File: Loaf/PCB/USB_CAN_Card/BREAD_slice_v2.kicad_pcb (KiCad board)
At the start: 2 copper layers, 100 x 70.6 mm, 8 parts, among them J1 10018783-10200TLF, U2 MCP3208

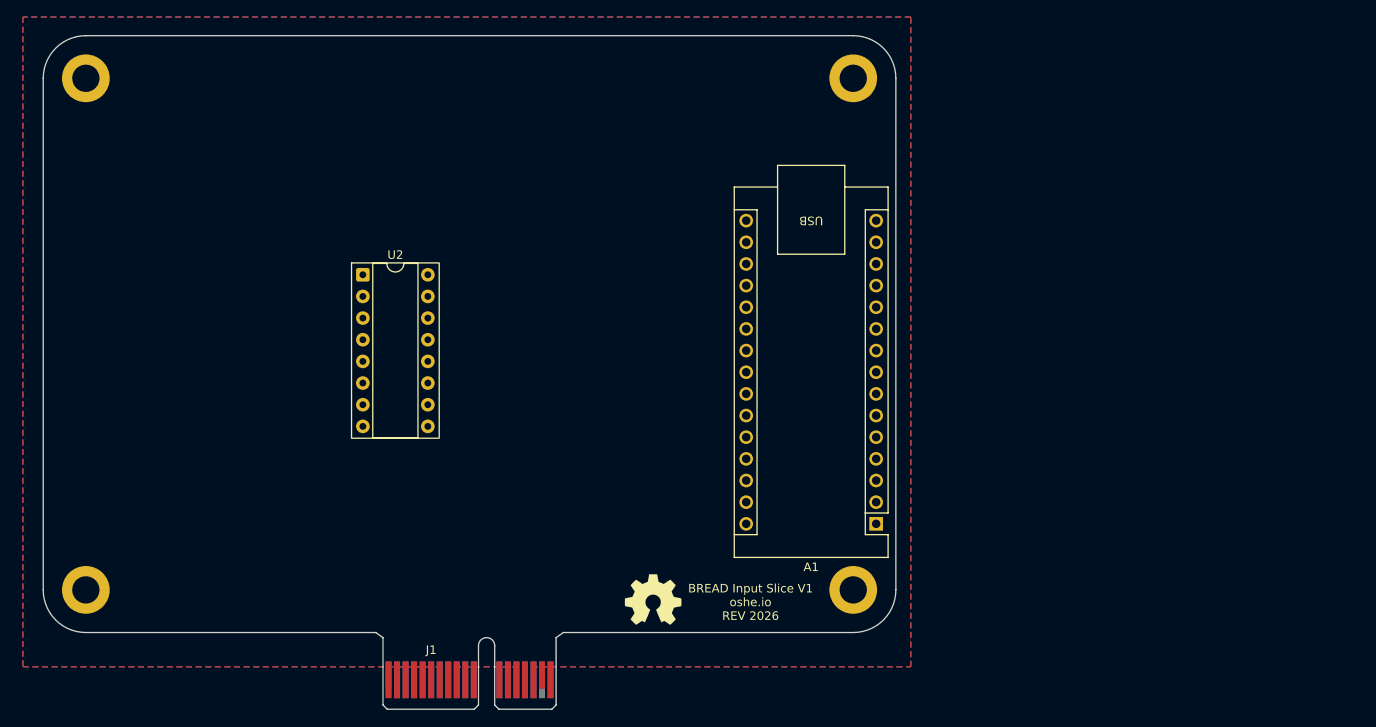
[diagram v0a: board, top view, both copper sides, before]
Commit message: Added parts to USB-CAN Card
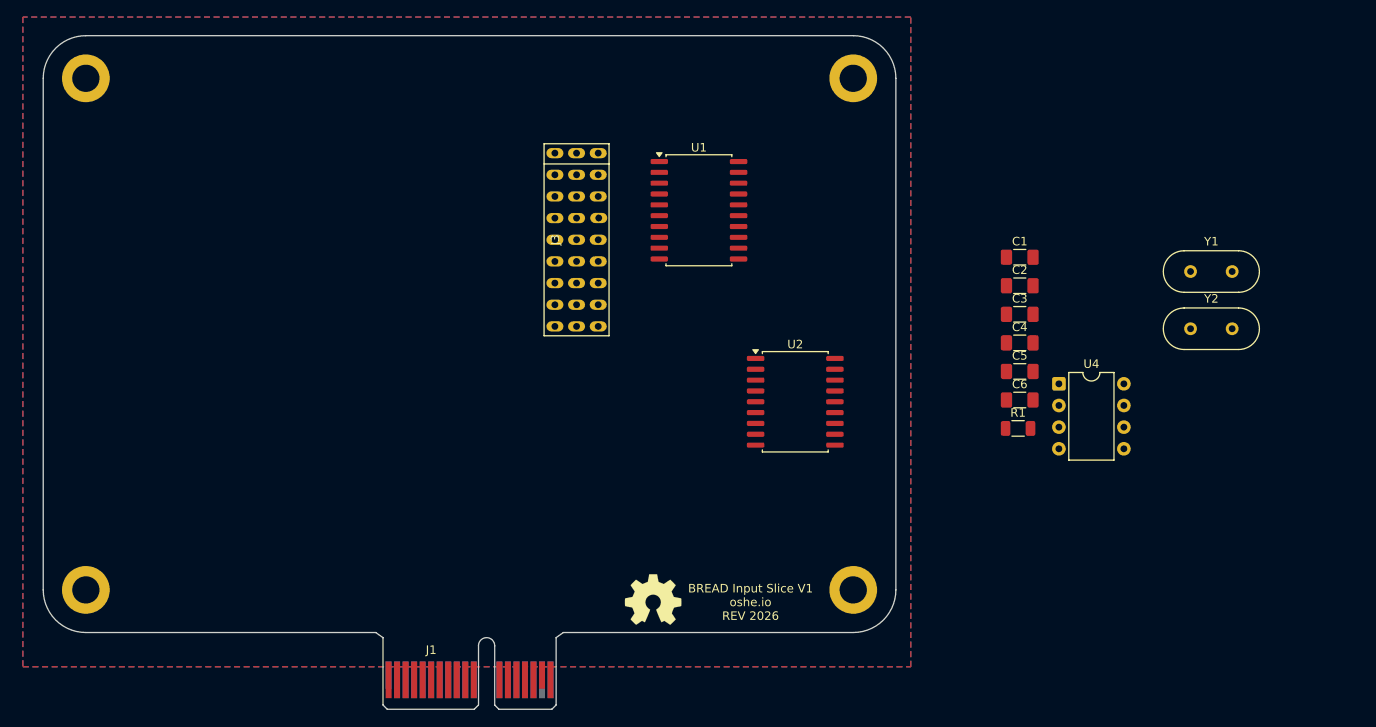
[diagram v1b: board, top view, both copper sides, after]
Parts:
- removed A1: Arduino_Nano_Every, Module:Arduino_Nano
- added C1: 22pF, Capacitor_SMD:C_1206_3216Metric_Pad1.33x1.80mm_HandSolder, F.Cu at (216.0, 81.5)
- added C2: 22pF, Capacitor_SMD:C_1206_3216Metric_Pad1.33x1.80mm_HandSolder, F.Cu at (216.0, 84.9)
- added C3: 0.2 - 0.47 uF, Capacitor_SMD:C_1206_3216Metric_Pad1.33x1.80mm_HandSolder, F.Cu at (216.0, 88.2)
- added C4: 22pF, Capacitor_SMD:C_1206_3216Metric_Pad1.33x1.80mm_HandSolder, F.Cu at (216.0, 91.6)
- added C5: 20pf, Capacitor_SMD:C_1206_3216Metric_Pad1.33x1.80mm_HandSolder, F.Cu at (216.0, 94.9)
- added C6: 20pf, Capacitor_SMD:C_1206_3216Metric_Pad1.33x1.80mm_HandSolder, F.Cu at (216.0, 98.3)
- added J3: ~, Custom:3x9 Jumper, F.Cu at (164.0, 79.5)
- added R1: 5.1k, Resistor_SMD:R_1206_3216Metric, F.Cu at (215.8, 101.6)
- added U1: MCP2210x-SO, Package_SO:SOIC-20W_7.5x12.8mm_P1.27mm, F.Cu at (178.3, 76.0)
- added U4: MCP2561-E-P, Package_DIP:DIP-8_W7.62mm, F.Cu at (220.6, 96.4)
- added Y1: 12MHZ Crystal, Crystal:Crystal_HC49-4H_Vertical, F.Cu at (236.0, 83.2)
- added Y2: 8 or 16MHZ Crystal, Crystal:Crystal_HC49-4H_Vertical, F.Cu at (236.0, 89.9)
- U2: value MCP3208 -> MCP2515-xSO; footprint Package_DIP:DIP-16_W7.62mm_Socket -> Package_SO:SOIC-18W_7.5x11.6mm_P1.27mm
- moved U2 52.9 mm to (189.7, 98.5)
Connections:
- net Net-(J2-Pin_1) renamed TXCAN
- net Net-(J3-Pin_1) renamed RXCAN
- U2 pad 10: ADC_CS -> unconnected-(U2-~{RX1BF}-Pad10)
- U2 pad 11: MOSI -> unconnected-(U2-~{RX0BF}-Pad11)
- U2 pad 12: MISO -> unconnected-(U2-~{INT}-Pad12)
- U2 pad 13: SPI_CLK -> SCLK
- U2 pad 14: GND -> MOSI
- U2 pad 15: +5V -> MISO
- U2 pad 16: +5V -> CS
- U2 pad 4: Net-(J5-Pin_1) -> unconnected-(U2-~{TX0RTS}-Pad4)
- U2 pad 7: unconnected-(U2-CH6-Pad7) -> Net-(U2-OSC2)

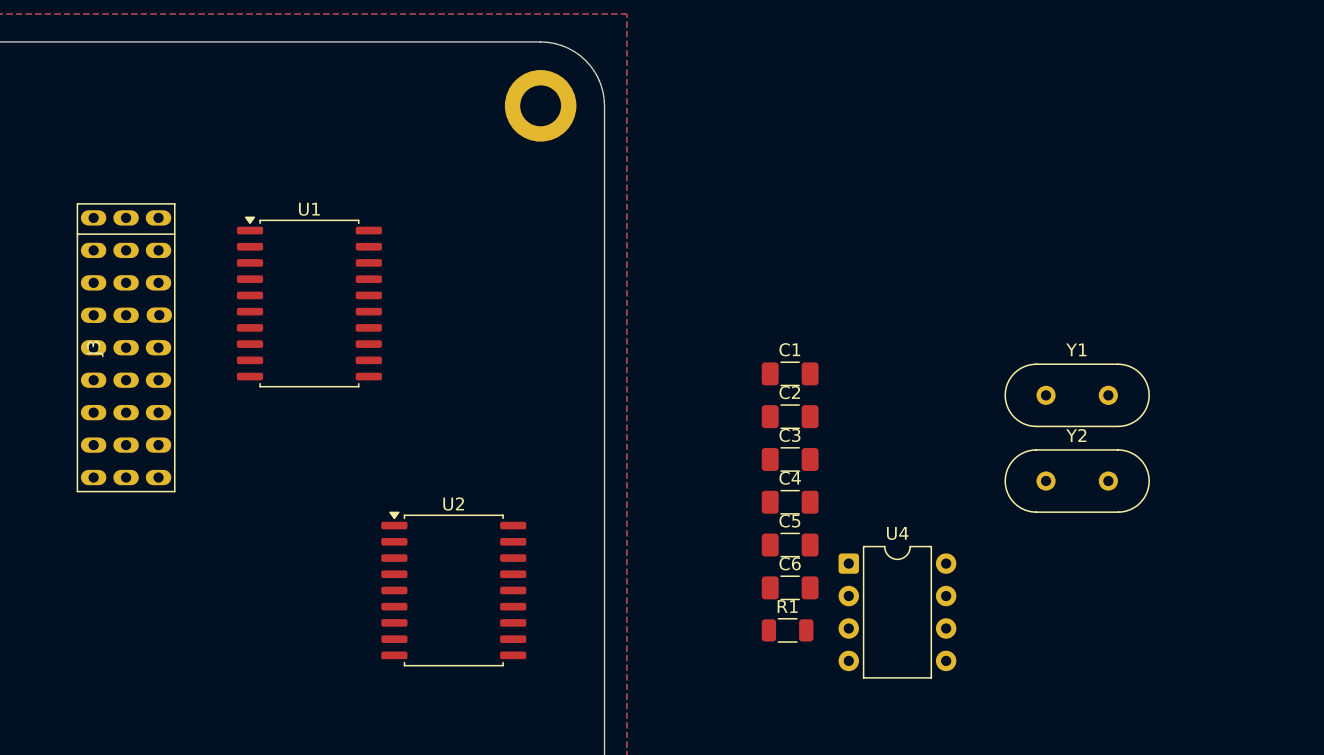
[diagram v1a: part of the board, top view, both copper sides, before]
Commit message: Updated IO slice schematic
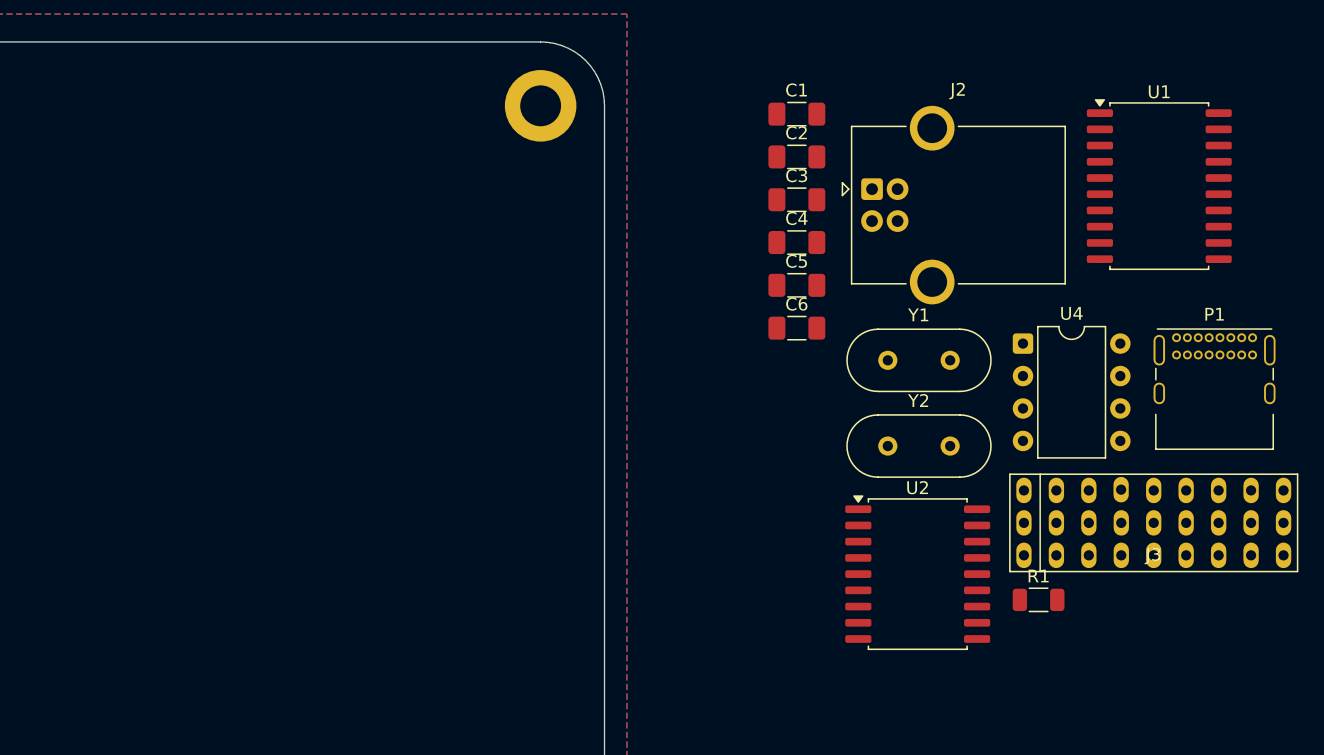
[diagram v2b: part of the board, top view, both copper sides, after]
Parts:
- added J2: USB_B, Connector_USB:USB_B_OST_USB-B1HSxx_Horizontal, F.Cu at (222.4, 67.0)
- added P1: USB_C_Plug_USB2.0, Connector_USB:USB_C_Receptacle_GCT_USB4085, F.Cu at (246.2, 78.7)
- moved J3 81.6 mm to (244.4, 93.2), turned to 0 degrees
- moved U1 67.2 mm to (244.9, 66.8)
- moved U2 36.3 mm to (226.0, 97.2)
- moved U4 22.0 mm to (234.2, 79.1)
- moved C4 20.3 mm to (216.5, 71.2)
- moved C1 20.3 mm to (216.5, 61.2)
- moved C2 20.3 mm to (216.5, 64.5)
- moved C3 20.3 mm to (216.5, 67.9)
- moved C5 20.3 mm to (216.5, 74.6)
- moved C6 20.3 mm to (216.5, 77.9)
- moved R1 19.8 mm to (235.4, 99.2)
- moved Y1 12.7 mm to (223.6, 80.4)
- moved Y2 12.7 mm to (223.6, 87.2)

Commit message: USB Slice and slop test program
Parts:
- removed J3: ~, Custom:3x9 Jumper
- removed P1: USB_C_Plug_USB2.0, Connector_USB:USB_C_Receptacle_GCT_USB4085
- removed R1: 5.1k, Resistor_SMD:R_1206_3216Metric
- removed U4: MCP2561-E-P, Package_DIP:DIP-8_W7.62mm
- added C7: 0.47uF, Capacitor_SMD:C_1206_3216Metric_Pad1.33x1.80mm_HandSolder, F.Cu at (138.3, 111.8)
- added C8: 0.47uF, Capacitor_SMD:C_1206_3216Metric_Pad1.33x1.80mm_HandSolder, F.Cu at (148.8, 96.5)
- added R2: 10k, Resistor_SMD:R_1206_3216Metric_Pad1.30x1.75mm_HandSolder, F.Cu at (138.3, 109.3)
- added R3: 10k, Resistor_SMD:R_1206_3216Metric_Pad1.30x1.75mm_HandSolder, F.Cu at (152.3, 110.8)
- added U3: MCP2561-E-P, Package_DIP:DIP-8_W7.62mm, F.Cu at (152.3, 99.2)
- C1: value 22pF -> 0.2 - 0.47 uF
- C3: value 0.2 - 0.47 uF -> 20pf
- C4: value 22pF -> 20pf
- U2: footprint Package_SO:SOIC-18W_7.5x11.6mm_P1.27mm -> Package_DIP:DIP-18_W7.62mm
- Y2: value 8 or 16MHZ Crystal -> 16MHZ Crystal
- moved U1 118.1 mm to (126.9, 71.5), turned to 90 degrees
- moved P2 109.1 mm to (113.6, 74.4), turned to 180 degrees
- moved Y2 103.3 mm to (120.6, 94.6)
- moved C3 98.9 mm to (119.1, 84.8), turned to 180 degrees
- moved C1 98.8 mm to (118.7, 74.5), turned to -90 degrees
- moved C6 98.2 mm to (119.1, 90.4), turned to 180 degrees
- moved Y1 98.1 mm to (125.5, 80.6), turned to 180 degrees
- moved C5 90.8 mm to (127.1, 90.4)
- moved C4 90.5 mm to (127.1, 84.8), turned to 180 degrees
- moved C2 90.0 mm to (126.5, 63.7), turned to 180 degrees
- moved U2 86.4 mm to (139.6, 99.2), turned to -90 degrees
- moved Logo1 1.50 mm to (171.5, 121.7)
- renumbered J2 to P2
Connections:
- C1 pad 1: Net-(U2-OSC2) -> GND
- C1 pad 2: GND -> VBus
- C2 pad 1: Net-(U2-CLKOUT/SOF) -> GND
- C2 pad 2: GND -> Net-(U1-VUSB)
- C3 pad 1: GND -> Net-(U1-OSC1)
- C3 pad 2: VBus -> GND
- C4 pad 2: Net-(U1-VUSB) -> Net-(U1-OSC2)
- C5 pad 1: Net-(U1-OSC1) -> Net-(U2-OSC2)
- C6 pad 1: GND -> Net-(U2-OSC1)
- C6 pad 2: Net-(U1-OSC2) -> GND
- U1 pad 10: Net-(U1-GP4) -> INT
- U1 pad 12: Net-(U1-GP5) -> unconnected-(U1-GP5-Pad12)
- U1 pad 14: Net-(U1-GP6) -> unconnected-(U1-GP6-Pad14)
- U1 pad 15: Net-(U1-GP7) -> unconnected-(U1-GP7-Pad15)
- U1 pad 16: Net-(U1-GP8) -> unconnected-(U1-GP8-Pad16)
- U1 pad 5: Net-(U1-GP0) -> unconnected-(U1-GP0-Pad5)
- U1 pad 6: Net-(U1-GP1) -> unconnected-(U1-GP1-Pad6)
- U1 pad 7: Net-(U1-GP2) -> unconnected-(U1-GP2-Pad7)
- U1 pad 8: Net-(U1-GP3) -> CS
- U2 pad 1: TXCAN -> /CANTX
- U2 pad 12: unconnected-(U2-~{INT}-Pad12) -> INT
- U2 pad 17: unconnected-(U2-~{RESET}-Pad17) -> Net-(U2-~{RESET})
- U2 pad 2: RXCAN -> /CANRX
- U2 pad 3: Net-(U2-CLKOUT/SOF) -> unconnected-(U2-CLKOUT/SOF-Pad3)
- U2 pad 8: unconnected-(U2-OSC1-Pad8) -> Net-(U2-OSC1)
- Y2 pad 1: Net-(U2-OSC2) -> Net-(U2-OSC1)
- Y2 pad 2: Net-(U2-CLKOUT/SOF) -> Net-(U2-OSC2)
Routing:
- net SCLK: track 0.00 -> 88.7 mm, vias 0 -> 2
- net MISO: track 0.00 -> 88.3 mm, vias 0 -> 2
- net INT: track 0.00 -> 87.8 mm, vias 0 -> 2
- net VBus: track 0.00 -> 87.7 mm, vias 0 -> 7
- net CS: track 0.00 -> 87.6 mm, vias 0 -> 2
- net MOSI: track 0.00 -> 87.4 mm, vias 0 -> 2
- net +12V: track 0.00 -> 29.9 mm, vias 0 -> 3
- net GND: track 0.00 -> 27.7 mm, vias 0 -> 5
- net +5V: track 0.00 -> 26.7 mm, vias 0 -> 1
- net /CANH: track 0.00 -> 25.8 mm
- net /CANL: track 0.00 -> 25.8 mm, vias 0 -> 1
- net D-: track 0.00 -> 15.0 mm
- net D+: track 0.00 -> 14.9 mm
- net /CANTX: track 0.00 -> 13.8 mm
- net Net-(U1-OSC1): track 0.00 -> 9.48 mm
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- added copper zone on F.Cu, net GND
- removed copper zone on F.Cu, net +5V
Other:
- board text added: "BREAD USB Slice 2026 oshe.io REV 1.0"
- board text removed: "BREAD Input Slice V1 oshe.io REV 2026"

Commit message: Updated PCB Schematics
Added correct capacitor values and one missing resistor on USB card
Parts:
- added R4: 10k, Resistor_SMD:R_1206_3216Metric_Pad1.30x1.75mm_HandSolder, B.Cu at (122.7, 73.7)
- C1: value 0.2 - 0.47 uF -> 2uF
- C2: value 22pF -> 0.22-0.47uF
- C7, C8: value 0.47uF -> 0.1uF
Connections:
- U1 pad 4: unconnected-(U1-~{RST}-Pad4) -> Net-(U1-~{RST})
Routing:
- net VBus: track 87.7 -> 92.4 mm, vias 7 -> 8
- net Net-(U1-~{RST}): track 0.00 -> 3.15 mm, vias 0 -> 1
